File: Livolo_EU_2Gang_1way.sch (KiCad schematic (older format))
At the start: 51 parts, among them IC1 ATMEGA328P, U1 ATSHA204A, U2 RFM69CW, U3 MIC5205-3.3, U4 MCP16301

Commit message: cleaning
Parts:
- C13: footprint Capacitors_SMD:C_0805_HandSoldering -> Capacitors_SMD:C_0603_HandSoldering
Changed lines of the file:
@@
 F 0 "C13" H 3309 4465 70  0000 L BNN
 F 1 "100n" H 3310 4265 70  0000 L BNN
-F 2 "Capacitors_SMD:C_0805_HandSoldering" H 3240 4140 65  0001 L TNN
+F 2 "Capacitors_SMD:C_0603_HandSoldering" H 3240 4140 65  0001 L TNN
 F 3 "" H 3250 4350 60  0001 C CNN
 	1    3250 4350

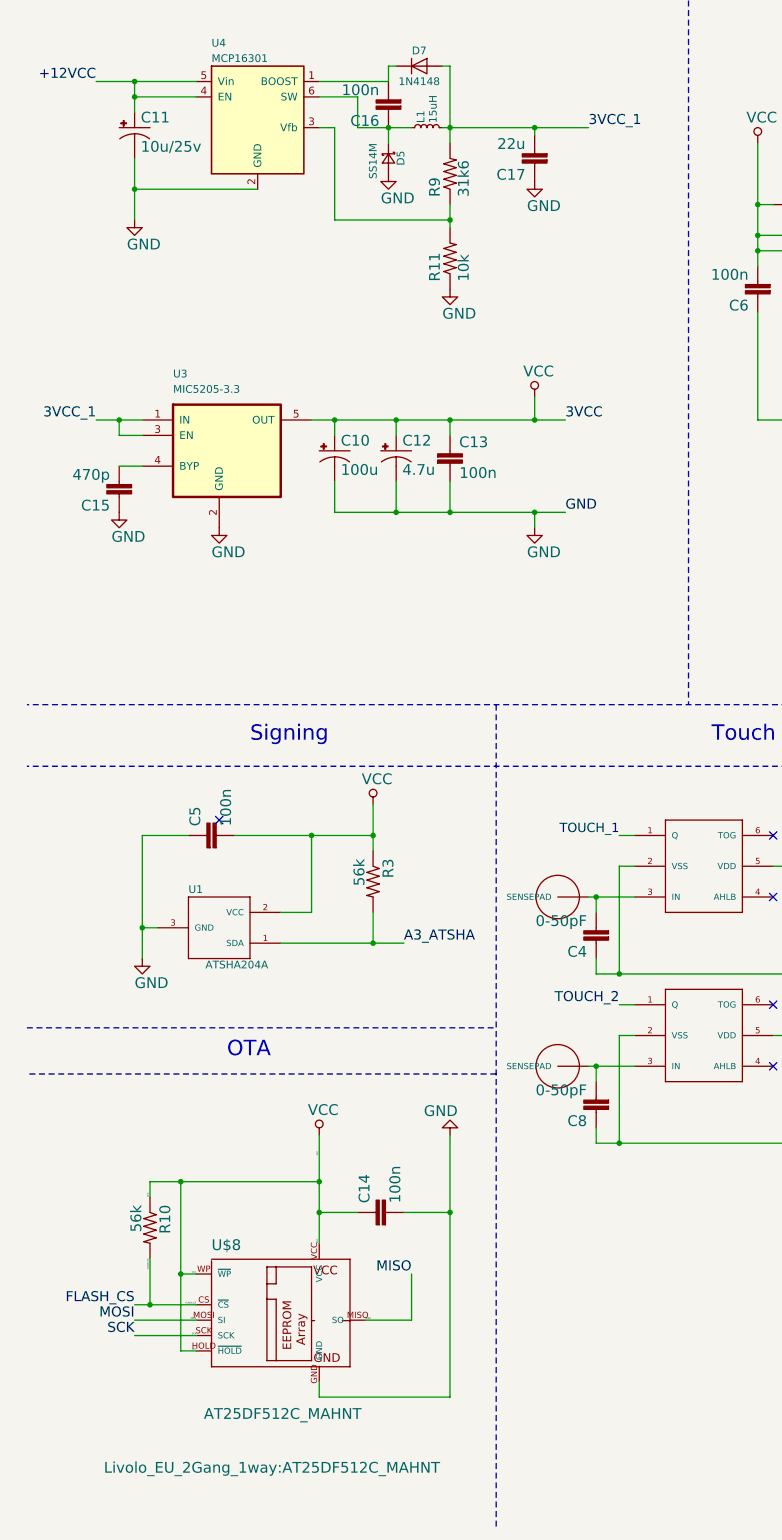
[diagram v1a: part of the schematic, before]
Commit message: replace bad footprint AT25DF512C
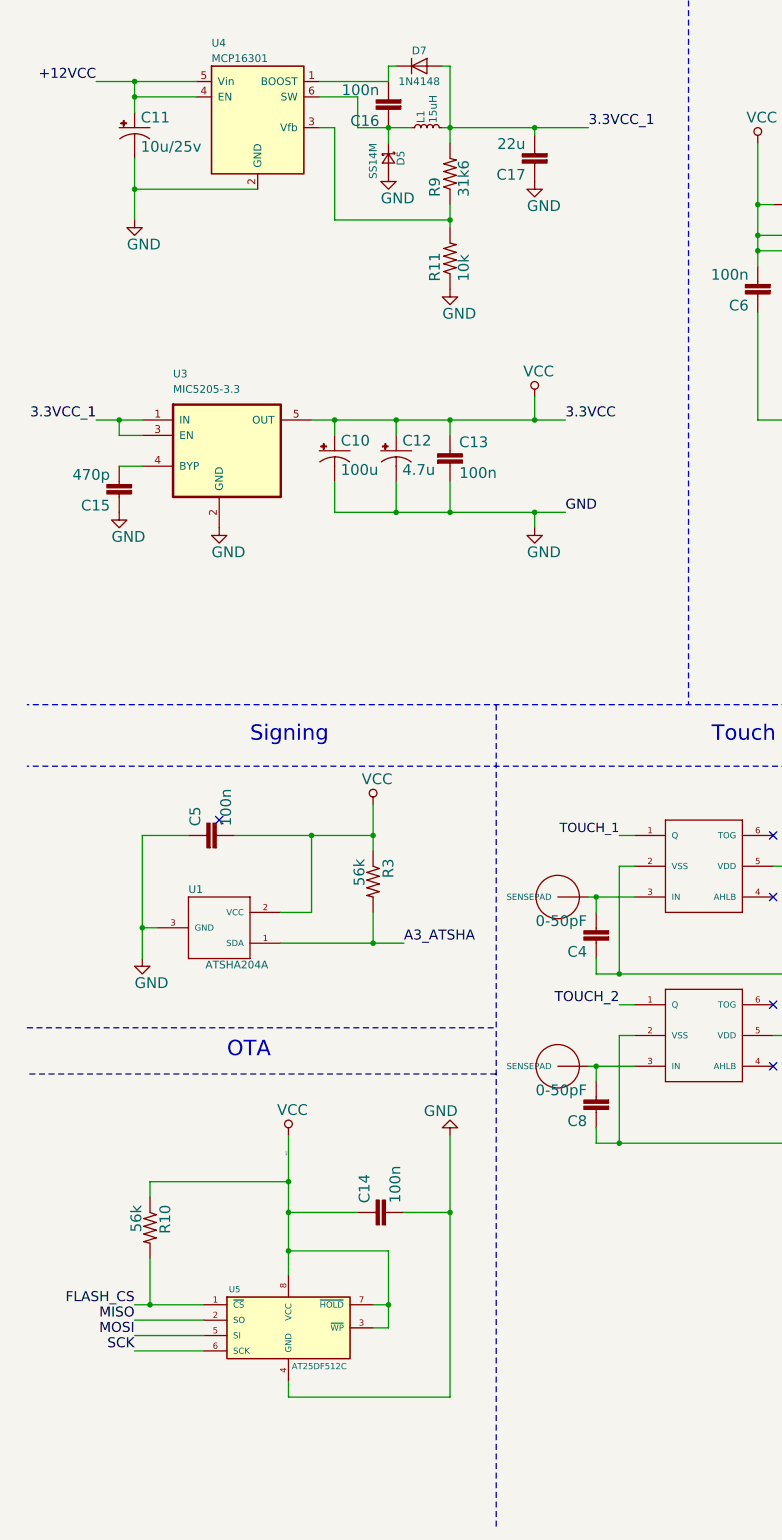
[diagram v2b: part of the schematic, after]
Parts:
- removed U$8: AT25DF512C_MAHNT, Livolo_EU_2Gang_1way:AT25DF512C_MAHNT, symbol AT25DF512C_MAHNT
- added U5: AT25DF512C, SOIC-8_3.9x4.9mm_Pitch1.27mm, symbol AT25DF512C
- U4: Part No (none) -> MCP16301T-I/CHY; Rating (none) -> 4-30V/3.3V/600mA
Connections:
- net FLASH_CS: now also U5.1 (~CS)
- net GND: now also U5.4 (GND)
- net MISO: now also U5.2 (SO)
- net MOSI: now also U5.5 (SI)
- net SCK: now also U5.6 (SCK)
- net VCC: now also U5.3 (~WP), U5.7 (~HOLD), U5.8 (VCC)
- net 3VCC_1 renamed 3.3VCC_1
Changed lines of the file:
@@
 LIBS:Livolo_EU_2Gang_1way
 LIBS:MIC5205
+LIBS:mysensors_memories
 LIBS:Livolo_EU_2Gang_1way-cache
 EELAYER 25 0
@@
 L VCC #SUPPLY021
 U 1 1 58DEFDDE
-P 2400 8700
-F 0 "#SUPPLY021" H 2326 8825 70  0001 L BNN
-F 1 "VCC" H 2326 8825 70  0000 L BNN
-F 2 "" H 2400 8700 60  0001 C CNN
-F 3 "" H 2400 8700 60  0001 C CNN
-	1    2400 8700
+P 2200 8700
+F 0 "#SUPPLY021" H 2126 8825 70  0001 L BNN
+F 1 "VCC" H 2126 8825 70  0000 L BNN
+F 2 "" H 2200 8700 60  0001 C CNN
+F 3 "" H 2200 8700 60  0001 C CNN
+	1    2200 8700
 	1    0    0    -1
 $EndComp
@@
 	1    15350 3750
 	0    -1   -1   0
-$EndComp
-$Comp
-L AT25DF512C_MAHNT U$8
-U 1 1 58DF0482
-P 2200 9900
-F 0 "U$8" H 1700 10347 70  0000 L BNN
-F 1 "AT25DF512C_MAHNT" H 1650 9250 70  0000 L BNN
-F 2 "Livolo_EU_2Gang_1way:AT25DF512C_MAHNT" H 1000 8900 70  0000 L BNN
-F 3 "" H 2200 9900 60  0001 C CNN
-	1    2200 9900
-	1    0    0    -1
 $EndComp
 $Comp
@@
 Text Label 13250 3950 0    65   ~ 0
 MISO
-Text Label 3000 9600 2    65   ~ 0
+Text Label 1200 9900 2    65   ~ 0
 MISO
 Text Label 13050 8050 2    65   ~ 0
@@
 Text Label 13250 3850 0    65   ~ 0
 MOSI
-Text Label 1200 9900 2    65   ~ 0
+Text Label 1200 10000 2    65   ~ 0
 MOSI
 Text Label 6300 2650 0    65   ~ 0
@@
 Text Label 13250 3750 0    65   ~ 0
 SCK
-Text Label 1200 10000 2    65   ~ 0
+Text Label 1200 10100 2    65   ~ 0
 SCK
 Text Label 4350 7850 2    65   ~ 0
@@
 Text Label 8450 2950 0    10   ~ 0
 A3_ATSHA
-Text Label 1300 9500 3    10   ~ 0
-FLASH_CS
-Text Label 1600 9800 2    10   ~ 0
-FLASH_CS
 Text Label 11750 7750 2    10   ~ 0
 GND
-Text Label 2700 9900 0    10   ~ 0
-MISO
-Text Label 1600 9900 2    10   ~ 0
-MOSI
-Text Label 1600 10000 2    10   ~ 0
-SCK
-Text Label 2400 8800 3    10   ~ 0
-VCC
-Text Label 2400 9400 1    10   ~ 0
-VCC
-Text Label 1600 10100 2    10   ~ 0
-VCC
-Text Label 1600 9600 2    10   ~ 0
-VCC
-Text Label 1300 9100 1    10   ~ 0
+Text Label 2200 8800 3    10   ~ 0
 VCC
 NoConn ~ 8450 3350
@@
 F 1 "MCP16301" H 1700 2600 50  0000 L CNN
 F 2 "TO_SOT_Packages_SMD:SOT-23-6" H 2000 1650 50  0001 C CNN
-F 3 "" H 1700 2700 50  0001 C CNN
+F 3 "http://www.farnell.com/datasheets/2129968.pdf" H 1700 2700 50  0001 C CNN
+F 4 "MCP16301T-I/CHY" H 2000 2150 60  0001 C CNN "Part No"
+F 5 "4-30V/3.3V/600mA" H 2000 2150 60  0001 C CNN "Rating"
 	1    2000 2150
 	1    0    0    -1
@@
 $EndComp
 Text Label 4150 2150 0    65   ~ 0
-3VCC_1
+3.3VCC_1
 Text Label 950  4050 2    65   ~ 0
-3VCC_1
+3.3VCC_1
 $Comp
 L CAP0402-CAP C15
@@
 $EndComp
 Text Label 4000 4050 0    65   ~ 0
-3VCC
+3.3VCC
 Text Label 4000 4650 0    65   ~ 0
 GND
@@
 Wire Bus Line
 	7850 7550 9350 7550
-Connection ~ 1500 9000
-Connection ~ 1500 9600
-Connection ~ 2400 9000
+Connection ~ 2200 9000
 Wire Wire Line
 	1300 9100 1300 9000
 Wire Wire Line
-	1600 9600 1500 9600
-Wire Wire Line
-	1500 10100 1600 10100
-Wire Wire Line
-	1500 9000 1500 10100
-Wire Wire Line
-	1300 9000 2400 9000
-Wire Wire Line
-	2400 8700 2400 9400
+	2200 8700 2200 9600
 Connection ~ 6050 6950
 Connection ~ 5750 8050
@@
 	4350 7850 4450 7850
 Wire Wire Line
-	1600 10000 1200 10000
+	1200 10000 1650 10000
 Wire Wire Line
 	14050 3750 13250 3750
@@
 	9350 4950 9850 4950
 Wire Wire Line
-	1600 9900 1200 9900
+	1200 9900 1650 9900
 Wire Wire Line
 	14050 3850 13250 3850
@@
 Wire Wire Line
 	13650 8050 13050 8050
-Wire Wire Line
-	3000 9900 3000 9600
-Wire Wire Line
-	2700 9900 3000 9900
 Wire Wire Line
 	14050 3950 13250 3950
@@
 Connection ~ 1300 9800
 Wire Wire Line
-	1200 9800 1600 9800
+	1200 9800 1650 9800
 Wire Wire Line
 	1300 9500 1300 9800
@@
 	2950 9200 3250 9200
 Wire Wire Line
-	2400 9200 2650 9200
-Connection ~ 2400 9200
-Wire Wire Line
-	3250 10400 2400 10400
+	2200 9200 2650 9200
+Connection ~ 2200 9200
 Connection ~ 3250 9200
-Wire Wire Line
-	2400 10400 2400 10300
 Connection ~ 1200 1850
 Wire Wire Line
@@
 	3800 4750 3800 4650
 NoConn ~ 11750 7550
+$Comp
+L AT25DF512C U5
+U 1 1 58E9D1C8
+P 2200 9950
+F 0 "U5" H 1850 10200 40  0000 C CNN
+F 1 "AT25DF512C" H 2400 9700 40  0000 C CNN
+F 2 "SOIC-8_3.9x4.9mm_Pitch1.27mm" H 2200 9950 30  0001 C CIN
+F 3 "" H 2200 9950 60  0000 C CNN
+	1    2200 9950
+	1    0    0    -1
+$EndComp
+Wire Wire Line
+	1200 10100 1650 10100
+Wire Wire Line
+	1300 9000 2200 9000
+Wire Wire Line
+	2200 9450 2850 9450
+Connection ~ 2200 9450
+Wire Wire Line
+	2850 9450 2850 9950
+Wire Wire Line
+	2850 9800 2750 9800
+Wire Wire Line
+	2850 9950 2750 9950
+Connection ~ 2850 9800
+Wire Wire Line
+	2200 10300 2200 10400
+Wire Wire Line
+	2200 10400 3250 10400
 $EndSCHEMATC

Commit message: Replace some capacitor 0402 -> 0603
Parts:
- C10, C12, C13: Rating (none) -> X5R/10V
- C15, C16, C17: footprint Capacitors_SMD:C_0402 -> Capacitors_SMD:C_0603
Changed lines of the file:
@@
 F 2 "Livolo_EU_2Gang_1way:EIA3216" H 2490 4040 65  0001 L TNN
 F 3 "" H 2500 4250 60  0001 C CNN
+F 4 "X5R/10V" H 2500 4250 60  0001 C CNN "Rating"
 	1    2500 4250
 	1    0    0    -1
@@
 F 2 "Livolo_EU_2Gang_1way:EIA3216" H 2890 4040 65  0001 L TNN
 F 3 "" H 2900 4250 60  0001 C CNN
+F 4 "X5R/10V" H 2900 4250 60  0001 C CNN "Rating"
 	1    2900 4250
 	1    0    0    -1
@@
 F 2 "Capacitors_SMD:C_0603_HandSoldering" H 3240 4140 65  0001 L TNN
 F 3 "" H 3250 4350 60  0001 C CNN
+F 4 "X5R/10V" H 3250 4350 60  0001 C CNN "Rating"
 	1    3250 4350
 	1    0    0    -1
@@
 F 0 "C16" H 2909 2065 70  0000 L BNN
 F 1 "100n" H 2910 1865 70  0000 L BNN
-F 2 "Capacitors_SMD:C_0402" H 2840 1740 65  0001 L TNN
+F 2 "Capacitors_SMD:C_0603" H 2840 1740 65  0001 L TNN
 F 3 "" H 2850 1950 60  0001 C CNN
 	1    2850 1950
@@
 F 0 "C17" H 3859 2415 70  0000 L BNN
 F 1 "22u" H 3860 2215 70  0000 L BNN
-F 2 "Capacitors_SMD:C_0402" H 3790 2090 65  0001 L TNN
+F 2 "Capacitors_SMD:C_0603" H 3790 2090 65  0001 L TNN
 F 3 "" H 3800 2300 60  0001 C CNN
 	1    3800 2300
@@
 F 0 "C15" H 1159 4565 70  0000 L BNN
 F 1 "470p" H 1160 4365 70  0000 L BNN
-F 2 "Capacitors_SMD:C_0402" H 1090 4240 65  0001 L TNN
+F 2 "Capacitors_SMD:C_0603" H 1090 4240 65  0001 L TNN
 F 3 "" H 1100 4450 60  0001 C CNN
 	1    1100 4450

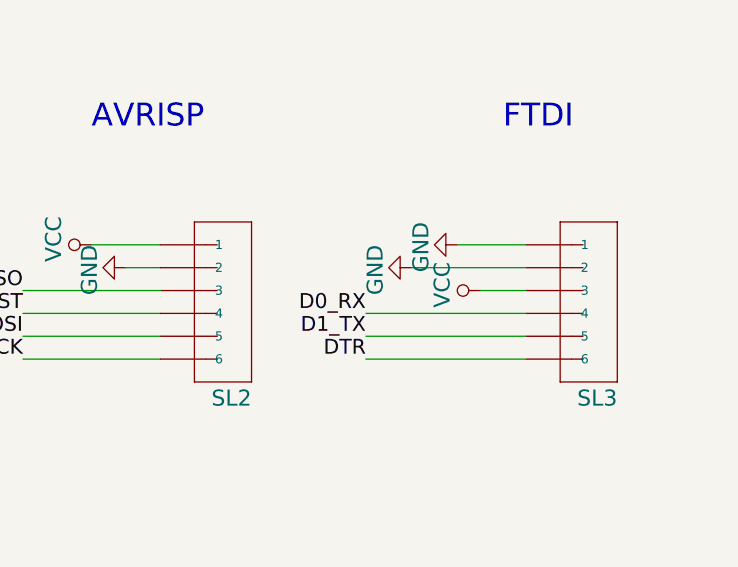
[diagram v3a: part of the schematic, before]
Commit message: Change FTDI wiring
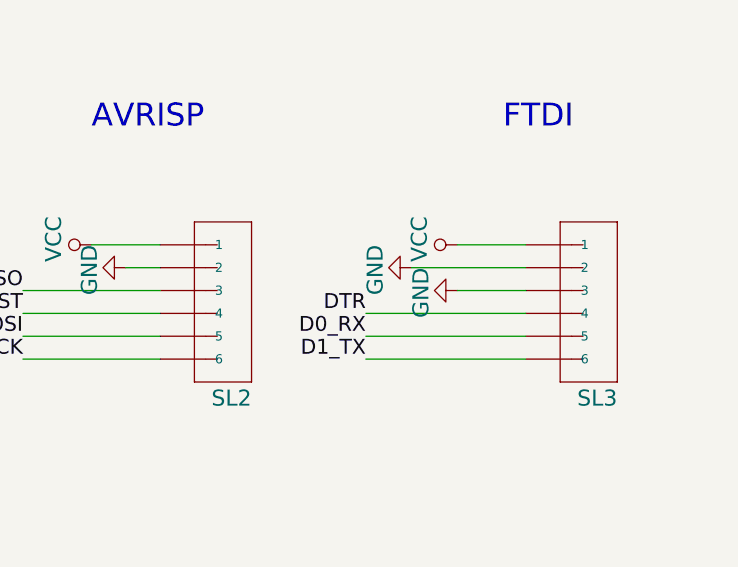
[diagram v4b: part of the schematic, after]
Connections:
- net D0_RX: now also SL3.5; no longer SL3.4
- net D1_TX: now also SL3.6; no longer SL3.5
- net DTR: now also SL3.4; no longer SL3.6
- net GND: now also SL3.3; no longer SL3.1
- net VCC: now also SL3.1; no longer SL3.3
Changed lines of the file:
@@
 L GND #GND06
 U 1 1 58DEECAE
-P 14950 7650
-F 0 "#GND06" H 14851 7550 70  0001 L BNN
-F 1 "GND" H 14850 7450 70  0000 L BNN
-F 2 "" H 14950 7650 60  0001 C CNN
-F 3 "" H 14950 7650 60  0001 C CNN
-	1    14950 7650
+P 14950 7850
+F 0 "#GND06" H 14851 7750 70  0001 L BNN
+F 1 "GND" H 14850 7650 70  0000 L BNN
+F 2 "" H 14950 7850 60  0001 C CNN
+F 3 "" H 14950 7850 60  0001 C CNN
+	1    14950 7850
 	0    1    1    0
 $EndComp
@@
 L VCC #SUPPLY014
 U 1 1 58DEFABE
-P 15050 7850
-F 0 "#SUPPLY014" H 14975 7975 70  0001 L BNN
-F 1 "VCC" H 14975 7975 70  0000 L BNN
-F 2 "" H 15050 7850 60  0001 C CNN
-F 3 "" H 15050 7850 60  0001 C CNN
-	1    15050 7850
+P 14950 7650
+F 0 "#SUPPLY014" H 14875 7775 70  0001 L BNN
+F 1 "VCC" H 14875 7775 70  0000 L BNN
+F 2 "" H 14950 7650 60  0001 C CNN
+F 3 "" H 14950 7650 60  0001 C CNN
+	1    14950 7650
 	0    -1   -1   0
 $EndComp
@@
 Text Label 8950 4650 2    65   ~ 0
 CSN
-Text Label 14550 7950 2    65   ~ 0
+Text Label 14550 8050 2    65   ~ 0
 D0_RX
 Text Label 8950 3550 2    65   ~ 0
 D0_RX
-Text Label 14550 8050 2    65   ~ 0
+Text Label 14550 8150 2    65   ~ 0
 D1_TX
 Text Label 8950 3650 2    65   ~ 0
@@
 Text Label 6150 2050 0    65   ~ 0
 DTR
-Text Label 14550 8150 2    65   ~ 0
+Text Label 14550 7950 2    65   ~ 0
 DTR
 Text Label 8950 4450 2    65   ~ 0
@@
 	13450 2750 13450 3450
 Wire Wire Line
-	15050 7850 15250 7850
+	14950 7850 15250 7850
 Wire Wire Line
 	13350 7650 13650 7650

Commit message: Change RFM69 by NRF24L01 cause crash
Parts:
- removed C1: 100n, Capacitors_SMD:C_0402, symbol CAP0402-CAP
- removed SL3: ~, Livolo_EU_2Gang_1way:1X06-1MM, symbol M06SMD-1MM
- removed U$3: 8MHZ, Livolo_EU_2Gang_1way:RESONATOR-SMD, symbol RESONATORSMD
- removed U$7: ANT, Livolo_EU_2Gang_1way:RFM12B-ANTENNA, symbol RFM12B_ANTENNA
- removed U2: RFM69CW, Livolo_EU_2Gang_1way:RFM69CW_MINIMAL, symbol RFM69_MINIMAL
- added L2: Ferrite_Bead, Resistors_SMD:R_0603_HandSoldering, symbol Ferrite_Bead
- added R12, R13: *1, Resistors_SMD:R_0603_HandSoldering, symbol RESISTOR0603-RES
- added U2: NRF24L01, Livolo:NRF24L01-SMD, symbol NRF24L01
- C2: footprint Capacitors_SMD:C_0603_HandSoldering -> Capacitors_SMD:C_0402
- C3: value 10u -> 4.7u
- U5: footprint SOIC-8_3.9x4.9mm_Pitch1.27mm -> Housings_SOIC:SOIC-8_3.9x4.9mm_Pitch1.27mm
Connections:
- net D1_TX is gone; now on net LED1: IC1.31 (PD1(TXD))
- net 3.3VCC_1: now also R12.2
- net CSN: now also U2.4 (CSN)
- net GND: now also C3.1, U2.1 (GND); no longer C3.2
- net IRQ: now also U2.8 (IRQ)
- net L1_RST: now also IC1.2 (PD4(XCK/T0)); no longer IC1.1 (PD3(INT1))
- net L1_SET: now also IC1.9 (PD5(T1)); no longer IC1.13 (PB1(OC1A))
- net L2_RST: now also IC1.28 (PC5(ADC5/SCL)); no longer IC1.11 (PD7(AIN1))
- net L2_SET: now also IC1.27 (PC4(ADC4/SDA)); no longer IC1.10 (PD6(AIN0))
- net LED1: no longer IC1.24 (PC1(ADC1))
- net LED2: now also IC1.24 (PC1(ADC1)); no longer IC1.9 (PD5(T1))
- net MISO: now also U2.7 (MISO)
- net MOSI: now also U2.6 (MOSI)
- net SCK: now also U2.5 (SCK)
- net VCC: now also C3.2, L2.1, U2.2 (VCC); no longer C10.+, C12.+, C13.1, C3.1, U3.5 (OUT)
- net 3.3VCC-Liv: now reaches U$2.2
- net 3.3VCC-Liv: now also R12.1, R13.1
- net A2: no longer names the net of IC1.25 (PC2(ADC2))
- net D0_RX: no longer names the net of IC1.30 (PD0(RXD))
- net TOUCH_1 renamed TOUCH_R
- net TOUCH_R: now also IC1.23 (PC0(ADC0)); no longer IC1.2 (PD4(XCK/T0))
- net TOUCH_2 renamed TOUCH_L
- net TOUCH_L: now also IC1.1 (PD3(INT1)); no longer IC1.23 (PC0(ADC0))
- new net: C10.+, C12.+, C13.1, L2.2, R13.2, U3.5 (OUT)
- new net CE: IC1.13 (PB1(OC1A)), U2.3 (CE)
- no-connect marks 17 -> 20
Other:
- note removed: "FTDI"
- moved on the sheet: C10, C12, C13, C3, R4

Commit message: replace TTP223 by MTCH105
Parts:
- removed C11: 10u/25v, Livolo_EU_2Gang_1way:EIA3216, symbol 10UF-POLAR-EIA3216-16V-10%_TANT_
- removed C14, C7, C9: 100n, Capacitors_SMD:C_0603_HandSoldering, symbol CAP0603-CAP
- removed C15: 470p, Capacitors_SMD:C_0603, symbol CAP0402-CAP
- removed C16: 100n, Capacitors_SMD:C_0603, symbol CAP0402-CAP
- removed C17: 22u, Capacitors_SMD:C_0603, symbol CAP0402-CAP
- removed C4, C8: 0-50pF, Capacitors_SMD:C_0603_HandSoldering, symbol CAP0603-CAP
- removed D5: SS14M, Livolo:SS14M, symbol D_Schottky_Small
- removed D7: 1N4148, Diodes_SMD:D_SOD-123, symbol 1N4148
- removed L1: 15uH, Livolo:VLCF4020T-150MR68, symbol L_Small
- removed R10: 56k, Resistors_SMD:R_0603_HandSoldering, symbol RESISTOR0603-RES
- removed R11: 10k, Resistors_SMD:R_0603_HandSoldering, symbol RESISTOR0603-RES
- removed R12, R13: *1, Resistors_SMD:R_0603_HandSoldering, symbol RESISTOR0603-RES
- removed R9: 31k6, Resistors_SMD:R_0603_HandSoldering, symbol RESISTOR0603-RES
- removed U$1, U$5: SENSOR_PAD_ROUND, Livolo:touch_pad_16mm, symbol SENSOR_PAD_ROUND
- removed U$4, U$6: TTP223-BA6, TO_SOT_Packages_SMD:SOT-23-6, symbol TTP223-BA6
- removed U3: MIC5205-3.3, TO_SOT_Packages_SMD:SOT-23-5_HandSoldering, symbol MIC5205-3.3YM5TR
- removed U4: MCP16301, TO_SOT_Packages_SMD:SOT-23-6, symbol MCP16301
- removed U5: AT25DF512C, Housings_SOIC:SOIC-8_3.9x4.9mm_Pitch1.27mm, symbol AT25DF512C
- added C1: 100n, Capacitors_SMD:C_0603_HandSoldering, symbol C_Small
- added C4: 1uF, Capacitors_SMD:C_0603_HandSoldering, symbol C_Small
- added R14, R16: 4K7, Resistors_SMD:R_0603, symbol R_Small
- added R15, R17: 0, Resistors_SMD:R_0603, symbol R_Small
- added R18, R19, R20: 10K, Resistors_SMD:R_0603, symbol R_Small
- added U6, U7: Touch, Livolo:livolo_ts_guard, symbol Touch
- added U8: MTCH105, Housings_SSOP:SSOP-14_5.3x6.2mm_Pitch0.65mm, symbol MTCH105
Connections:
- net 3.3VCC-Liv: now also C10.+, C12.+, C13.1, L2.2
- net A3_ATSHA: no longer IC1.26 (PC3(ADC3))
- net GND: now also C1.1, C4.2, U8.10 (MTO2/GC), U8.14 (VSS)
- net L2_RST: now also IC1.27 (PC4(ADC4/SDA)); no longer IC1.28 (PC5(ADC5/SCL))
- net L2_SET: now also IC1.26 (PC3(ADC3)); no longer IC1.27 (PC4(ADC4/SDA))
- net LED1: now also IC1.10 (PD6(AIN0)); no longer IC1.31 (PD1(TXD))
- net TOUCH_L: now also R20.2, U8.12 (MTO1)
- net TOUCH_R: now also R18.2, U8.13 (MTO0)
- net VCC: now also C1.2, R18.1, R20.1, U8.1 (VDD)
- net MTPM: now reaches IC1.11 (PD7(AIN1))
- net MTPM: now also U8.4 (MTPM)
- net BUZZER: now reaches IC1.25 (PC2(ADC2))
- net BUZZER: now also U$2.8
- net +12VCC: no longer names the net of U$2.13
- net FLASH_CS: no longer names the net of IC1.12 (PB0(ICP))
- new net: C4.1, R19.2, U8.11 (MTSA)
- new net: R16.1, U8.2 (MTI0)
- new net: R14.1, U8.3 (MTI1)
- new net: R15.1, R17.1, U8.5 (MTI2/GUARD)
- new net: R14.2, U6.1 (TS)
- new net: R15.2, U6.2 (Guard)
- new net: R16.2, U7.1 (TS)
- new net: R17.2, U7.2 (Guard)
- new net MTSA: IC1.28 (PC5(ADC5/SCL)), R19.1
- no-connect marks 20 -> 19
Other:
- note removed: "OTA"
- moved on the sheet: C10, C12, C13, C3, C5, L2, R3, R4, U1, U2
